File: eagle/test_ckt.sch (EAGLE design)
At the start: 38 parts, among them IC1 LT1352PA, T1 2N3904, T2 2N3904

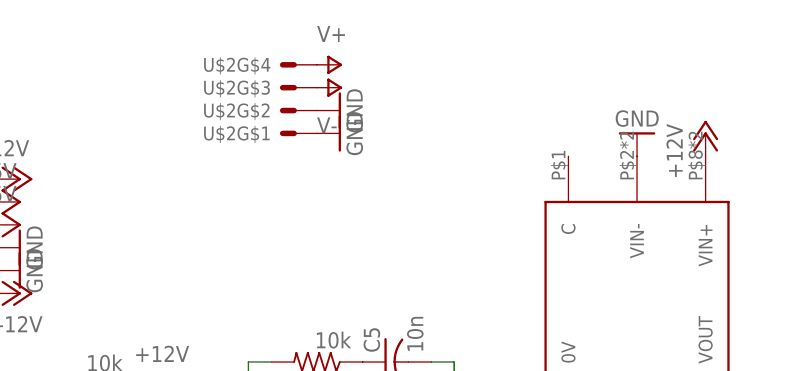
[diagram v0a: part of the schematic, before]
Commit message: Fix pin assignment minifit Jr
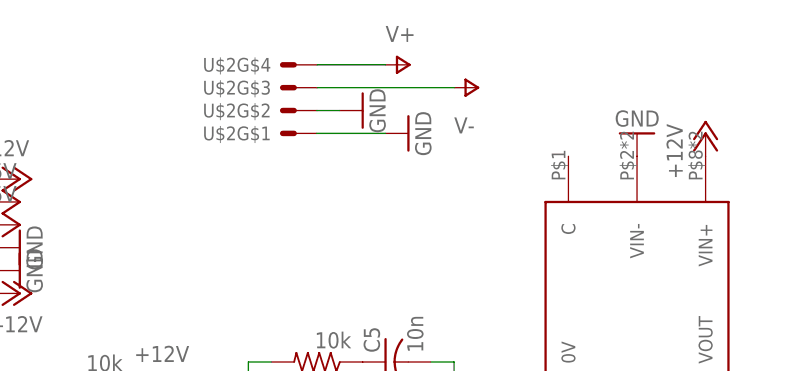
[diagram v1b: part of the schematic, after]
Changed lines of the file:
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@@
 <instance part="GND8" gate="1" x="96.52" y="104.14"/>
 <instance part="SV1" gate="1" x="22.86" y="144.78"/>
-<instance part="P+7" gate="1" x="73.66" y="162.56" rot="R270"/>
-<instance part="P-6" gate="1" x="73.66" y="160.02" rot="R90"/>
-<instance part="GND9" gate="1" x="73.66" y="157.48" rot="R90"/>
-<instance part="GND10" gate="1" x="73.66" y="154.94" rot="R90"/>
+<instance part="P+7" gate="1" x="81.28" y="162.56" rot="R270"/>
+<instance part="P-6" gate="1" x="88.9" y="160.02" rot="R90"/>
+<instance part="GND9" gate="1" x="76.2" y="157.48" rot="R90"/>
+<instance part="GND10" gate="1" x="81.28" y="154.94" rot="R90"/>
 <instance part="GND14" gate="1" x="190.5" y="106.68"/>
 <instance part="GND16" gate="1" x="38.1" y="139.7" rot="R90"/>
@@
 <pinref part="U$2" gate="G$2" pin="S"/>
 <pinref part="GND9" gate="1" pin="GND"/>
+<wire x1="73.66" y1="157.48" x2="71.12" y2="157.48" width="0.1524" layer="91"/>
 </segment>
 <segment>
 <pinref part="U$2" gate="G$1" pin="S"/>
 <pinref part="GND10" gate="1" pin="GND"/>
+<wire x1="78.74" y1="154.94" x2="71.12" y2="154.94" width="0.1524" layer="91"/>
 </segment>
 </net>
@@
 <pinref part="U$2" gate="G$4" pin="S"/>
 <pinref part="P+7" gate="1" pin="V+"/>
+<wire x1="78.74" y1="162.56" x2="71.12" y2="162.56" width="0.1524" layer="91"/>
 </segment>
 </net>
@@
 <pinref part="U$2" gate="G$3" pin="S"/>
 <pinref part="P-6" gate="1" pin="V-"/>
+<wire x1="86.36" y1="160.02" x2="71.12" y2="160.02" width="0.1524" layer="91"/>
 </segment>
 </net>
